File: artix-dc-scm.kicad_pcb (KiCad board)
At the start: 8 copper layers, 90 x 120.4 mm, 343 parts, among them IC1 TPS54561, J1 WE-RJ45_7499111121A, J10 61300611121, J11 DC_SOCKET, J12 S2B-PH-K-S_LF__SN_, J13 62000311121, J2 1-2199230-6, J3 543630489, J4 M20-7830642, J5 SFF-TA-1002-4C+, J6 0878311420, J7 61301021121, J8 61301021121, J9 61301221121, Q1 IRLML6402TRPBF, Q10 2N7002, Q11 2N7002, Q2 IRLML6402TRPBF, Q3 IRLML6402TRPBF, Q4 IRLML6402TRPBF, Q5 IRLML6402TRPBF, Q6 IRLML6402TRPBF, Q7 2N7002, Q8 2N7002, Q9 2N7002, U1 KSZ9031RNXCA, U10 TPS62823DLCT, U11 TPS62823DLCT, U12 TPS62823DLCT, U13 TPS62823DLCT, U14 XC7A100T-FGG484, U15 SN74LVC1G08DCKR, U15 TPS62823DLCT, U16 LM21212-2, U16 SN74LS08DBR, U2 W25Q32JVSSIQ_TR, U3 W25Q32JVSSIQ_TR, U4 W25Q32JVSSIQ_TR, U5 W25Q32JVSSIQ_TR, U6 NVT2008DQ,115, U7 AS4C256M16D3, U8 TPS51200DRC, U9 LM3881MME_NOPB, Y1 ABM8G-25.000MHZ-18-D2Y-T

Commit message: Added DDR3 and FLASH layout
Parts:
- removed the R63 at (256.4, 54.4)
- removed the R64 at (274.4, 45.2)
- removed the R65 at (271.5, 47.2)
- removed the S1 at (253.3, 87.3)
- added C48: C_4u7_0402, antmicro-footprints:0402-cap, B.Cu at (76.4, 114.8)
- added C49: C_470n_0402, antmicro-footprints:0402-cap, B.Cu at (79.8, 114.8)
- added C50: C_470n_0402, antmicro-footprints:0402-cap, B.Cu at (84.7, 121.8)
- added C91: C_47u_1210, antmicro-footprints:1210-cap, F.Cu at (187.6, 67.1)
- C35, C36, C37, C38, C51, C52, C53, C54, C55, C56, C57, C58, C59, C60, C61, C62, R21, R22, R23, R24, R25, R26, R27, R28, R29, R30, R31, R32, R33, R34, R35, R36, R37, R38, R39, R40, R41, R42, R43, R44, R60: moved to B.Cu
- R63: renamed from C48; value C_4u7_0402 -> R_1k_0402; footprint antmicro-footprints:0402-cap -> antmicro-footprints:0402-res
- R64: renamed from C49; value C_470n_0402 -> R_1k_0402; footprint antmicro-footprints:0402-cap -> antmicro-footprints:0402-res
- R65: renamed from C50; value C_470n_0402 -> R_1k_0402; footprint antmicro-footprints:0402-cap -> antmicro-footprints:0402-res
- S1: renamed from C91; value C_47u_1210 -> KMR2; footprint antmicro-footprints:1210-cap -> antmicro-footprints:SW_SPST_4.2x2.8
- moved C52 188.7 mm to (78.6, 122.2), turned to 180 degrees
- moved C58 188.6 mm to (78.3, 110.3), turned to 90 degrees
- moved R60 188.4 mm to (79.8, 112.8)
- moved C62 186.0 mm to (84.7, 115.8), turned to 90 degrees
- moved R54 184.3 mm to (72.0, 116.0), turned to 180 degrees
- moved C60 181.3 mm to (78.3, 113.0), turned to 270 degrees
- moved C61 180.9 mm to (84.7, 117.8), turned to 90 degrees
- moved R55 180.2 mm to (72.0, 121.0), turned to 180 degrees
- moved C56 180.1 mm to (78.1, 120.8), turned to 270 degrees
- moved R56 179.0 mm to (72.0, 111.0), turned to 180 degrees
- moved C59 177.6 mm to (78.3, 118.5), turned to 90 degrees
- moved R62 176.9 mm to (89.0, 116.0), turned to 180 degrees
- moved C55 176.7 mm to (84.7, 112.8), turned to 270 degrees
- moved R61 174.9 mm to (89.0, 115.0)
- moved C53 174.2 mm to (78.3, 116.5), turned to 270 degrees
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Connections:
- net /Power supply 2/VCCAUX_EN_N renamed /Power supply/VCCAUX_EN_N
- net /Power supply 2/VCCINT_EN_N renamed /Power supply/VCCINT_EN_N
- net /Power supply 2/VCCIO_EN_N renamed /Power supply/VCCIO_EN_N
- net /Power supply 2/VR1_PG renamed /Power supply/VR1_PG
- net /Power supply 2/VR2_PG renamed /Power supply/VR2_PG
- net /Power supply 2/VR_GOOD renamed /Power supply/VR_GOOD
- Q10 pad 1: /Power supply 2/1V35_PG -> /Power supply/1V35_PG
- Q11 pad 1: /Power supply 2/2V5_PG -> /Power supply/2V5_PG
- Q7 pad 1: /Power supply 2/1V0_PG -> /Power supply/1V0_PG
- Q9 pad 1: /Power supply 2/1V8_PG -> /Power supply/1V8_PG
- R63 pad 1: VCC1V35 -> VCC3V3
- R63 pad 2: GND -> /Power supply/VCCINT_EN
- R64 pad 1: VCC1V35 -> VCC3V3
- R64 pad 2: GND -> /Power supply/VCCAUX_EN
- R65 pad 1: VCC1V35 -> VCC3V3
- R65 pad 2: GND -> /Power supply/VCCIO_EN
- R91 pad 2: /Power supply 2/1V0_PG -> /Power supply/1V0_PG
- R92 pad 1: /Power supply 2/PWR_EN -> /Power supply/PWR_EN
- R93 pad 2: /Power supply 2/1V8_PG -> /Power supply/1V8_PG
- R94 pad 2: /Power supply 2/1V35_PG -> /Power supply/1V35_PG
- R95 pad 2: /Power supply 2/2V5_PG -> /Power supply/2V5_PG
- S1 pad 1: VCCB13 -> PROGRAM
- U16 pad 10: /Power supply 2/1V35_PG -> /Power supply/1V35_PG
- U16 pad 12: /Power supply 2/1V0_PG -> /Power supply/1V0_PG
- U16 pad 13: /Power supply 2/3V3_PG -> /Power supply/3V3_PG
- U16 pad 6: /Power supply 2/PWR_EN -> /Power supply/PWR_EN
- U16 pad 9: /Power supply 2/1V8_PG -> /Power supply/1V8_PG
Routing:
- net VCC3V3: track 8.31 -> 20.1 mm, vias 3 -> 7
- net VCC1V35: track 2.88 -> 14.6 mm, vias 0 -> 6
- net QSPIB_CLK: track 0.00 -> 11.2 mm, vias 0 -> 2
- net QSPIA_CLK: track 0.00 -> 11.2 mm, vias 0 -> 2
- net GND: track 10.0 -> 19.6 mm, vias 0 -> 5
- net QSPIB2_CS_N: track 0.00 -> 9.11 mm, vias 0 -> 1
- net QSPIA2_CS_N: track 0.00 -> 8.10 mm, vias 0 -> 1
- net QSPIB1_CS_N: track 0.00 -> 8.10 mm, vias 0 -> 1
- net QSPIA1_CS_N: track 0.00 -> 8.10 mm, vias 0 -> 1
- net QSPIB2_D3: track 0.00 -> 7.56 mm, vias 0 -> 1
- net QSPIB1_D3: track 0.00 -> 7.56 mm, vias 0 -> 1
- net QSPIA2_D3: track 0.00 -> 7.56 mm, vias 0 -> 1
- net QSPIA1_D3: track 0.00 -> 7.56 mm, vias 0 -> 1
- net QSPIB2_D1: track 0.00 -> 6.41 mm, vias 0 -> 1
- net QSPIB1_D1: track 0.00 -> 6.41 mm, vias 0 -> 1
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
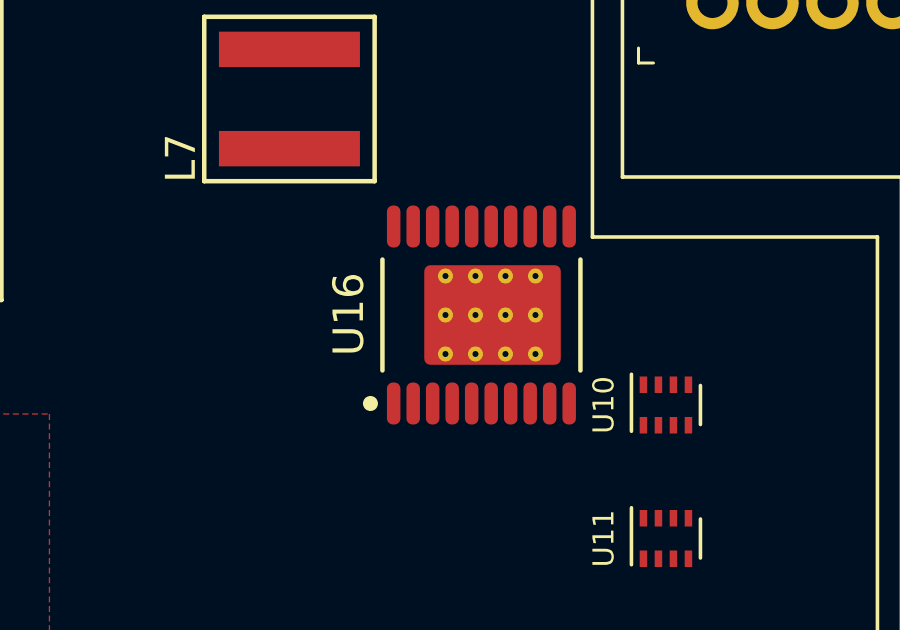
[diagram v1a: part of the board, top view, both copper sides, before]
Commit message: Updated board 3D models
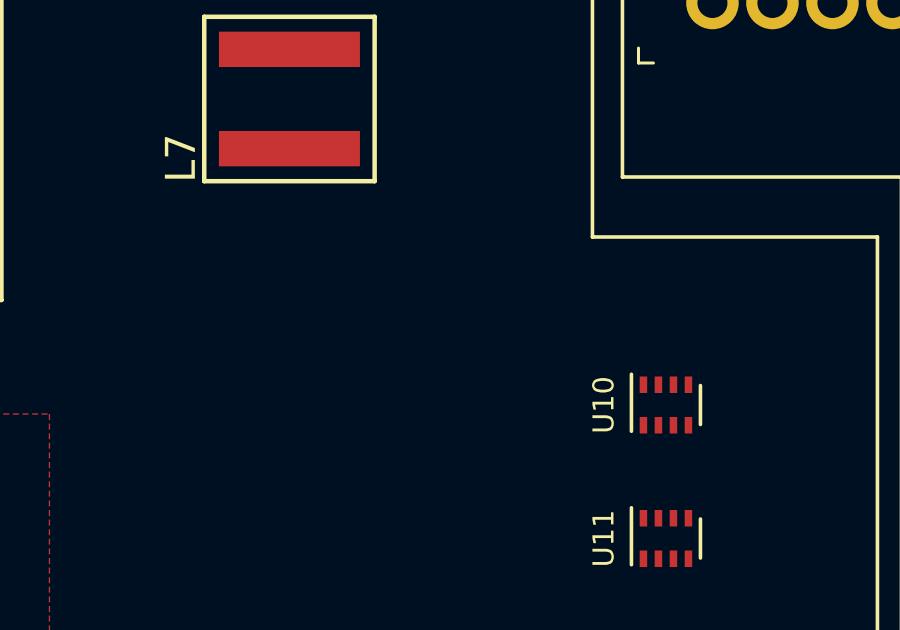
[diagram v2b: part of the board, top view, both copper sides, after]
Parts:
- removed the U16 at (92.3, 74.1)
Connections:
- J2 pad 1: GND -> (no net)
- J2 pad 10: Net-(D1-Pad2) -> (no net)
- J2 pad 11: Net-(J2-Pad11) -> (no net)
- J2 pad 12: VCC3V3 -> (no net)
- J2 pad 13: Net-(J2-Pad13) -> (no net)
- J2 pad 14: VCC3V3 -> (no net)
- J2 pad 15: GND -> (no net)
- J2 pad 16: VCC3V3 -> (no net)
- J2 pad 17: Net-(J2-Pad17) -> (no net)
- J2 pad 18: VCC3V3 -> (no net)
- J2 pad 19: Net-(J2-Pad19) -> (no net)
- J2 pad 2: VCC3V3 -> (no net)
- J2 pad 20: Net-(J2-Pad20) -> (no net)
- J2 pad 21: GND -> (no net)
- J2 pad 22: Net-(J2-Pad22) -> (no net)
- J2 pad 23: Net-(J2-Pad23) -> (no net)
- J2 pad 24: Net-(J2-Pad24) -> (no net)
- J2 pad 25: Net-(J2-Pad25) -> (no net)
- J2 pad 26: Net-(J2-Pad26) -> (no net)
- J2 pad 27: GND -> (no net)
- J2 pad 28: Net-(J2-Pad28) -> (no net)
- J2 pad 29: Net-(J2-Pad29) -> (no net)
- J2 pad 3: GND -> (no net)
- J2 pad 30: Net-(J2-Pad30) -> (no net)
- J2 pad 31: Net-(J2-Pad31) -> (no net)
- J2 pad 32: Net-(J2-Pad32) -> (no net)
- J2 pad 33: GND -> (no net)
- J2 pad 34: Net-(J2-Pad34) -> (no net)
- J2 pad 35: Net-(C30-Pad1) -> (no net)
- J2 pad 36: Net-(J2-Pad36) -> (no net)
- J2 pad 37: Net-(C28-Pad1) -> (no net)
- J2 pad 38: Net-(J2-Pad38) -> (no net)
- J2 pad 39: GND -> (no net)
- J2 pad 4: VCC3V3 -> (no net)
- J2 pad 40: Net-(J2-Pad40) -> (no net)
- J2 pad 41: PCIE_HPM_RXN[0] -> (no net)
- J2 pad 42: Net-(J2-Pad42) -> (no net)
- J2 pad 43: PCIE_HPM_RXP[0] -> (no net)
- J2 pad 44: Net-(J2-Pad44) -> (no net)
- J2 pad 45: GND -> (no net)
- J2 pad 46: Net-(J2-Pad46) -> (no net)
- J2 pad 47: Net-(C29-Pad1) -> (no net)
- J2 pad 48: Net-(J2-Pad48) -> (no net)
- J2 pad 49: Net-(C27-Pad1) -> (no net)
- J2 pad 5: Net-(J2-Pad5) -> (no net)
- J2 pad 50: PEX_L0_RST_N -> (no net)
- J2 pad 51: GND -> (no net)
- J2 pad 52: PEX_L0_CLKREQ_N -> (no net)
- J2 pad 53: CLK_100M_PCIE_DN -> (no net)
- J2 pad 54: PEWAKE_3V3_N -> (no net)
- J2 pad 55: CLK_100M_PCIE_DP -> (no net)
- J2 pad 56: Net-(J2-Pad56) -> (no net)
- J2 pad 57: GND -> (no net)
- J2 pad 58: Net-(J2-Pad58) -> (no net)
- J2 pad 6: Net-(J2-Pad6) -> (no net)
- J2 pad 67: Net-(J2-Pad67) -> (no net)
- J2 pad 68: Net-(J2-Pad68) -> (no net)
- J2 pad 69: Net-(J2-Pad69) -> (no net)
- J2 pad 7: Net-(J2-Pad7) -> (no net)
- J2 pad 70: VCC3V3 -> (no net)
- J2 pad 71: GND -> (no net)
- J2 pad 72: VCC3V3 -> (no net)
- J2 pad 73: GND -> (no net)
- J2 pad 74: VCC3V3 -> (no net)
- J2 pad 75: GND -> (no net)
- J2 pad 8: Net-(J2-Pad8) -> (no net)
- J2 pad 9: GND -> (no net)
- J2 pad SH1: GND -> (no net)
- J2 pad SH2: GND -> (no net)

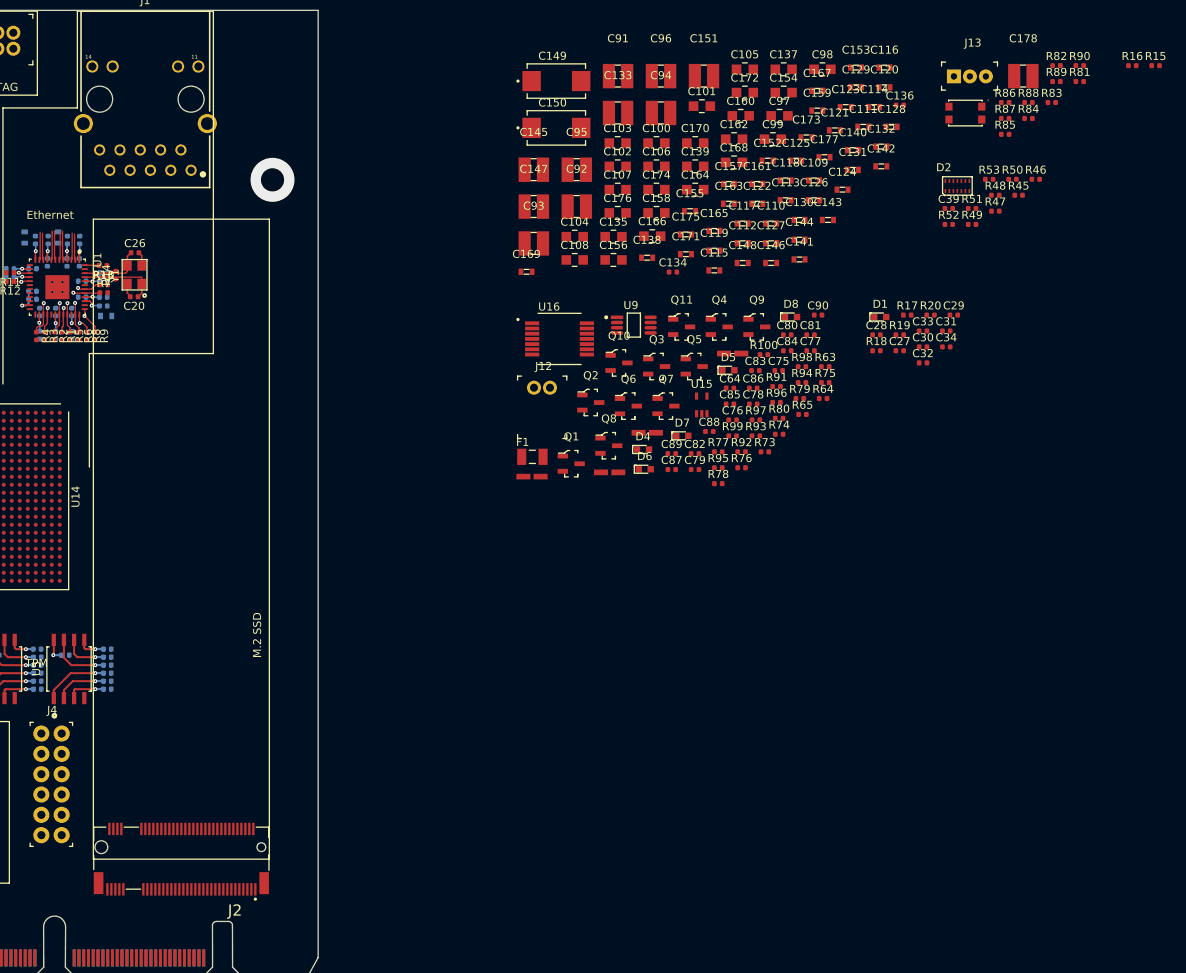
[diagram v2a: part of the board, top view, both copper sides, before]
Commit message: Added M.2 connector layout
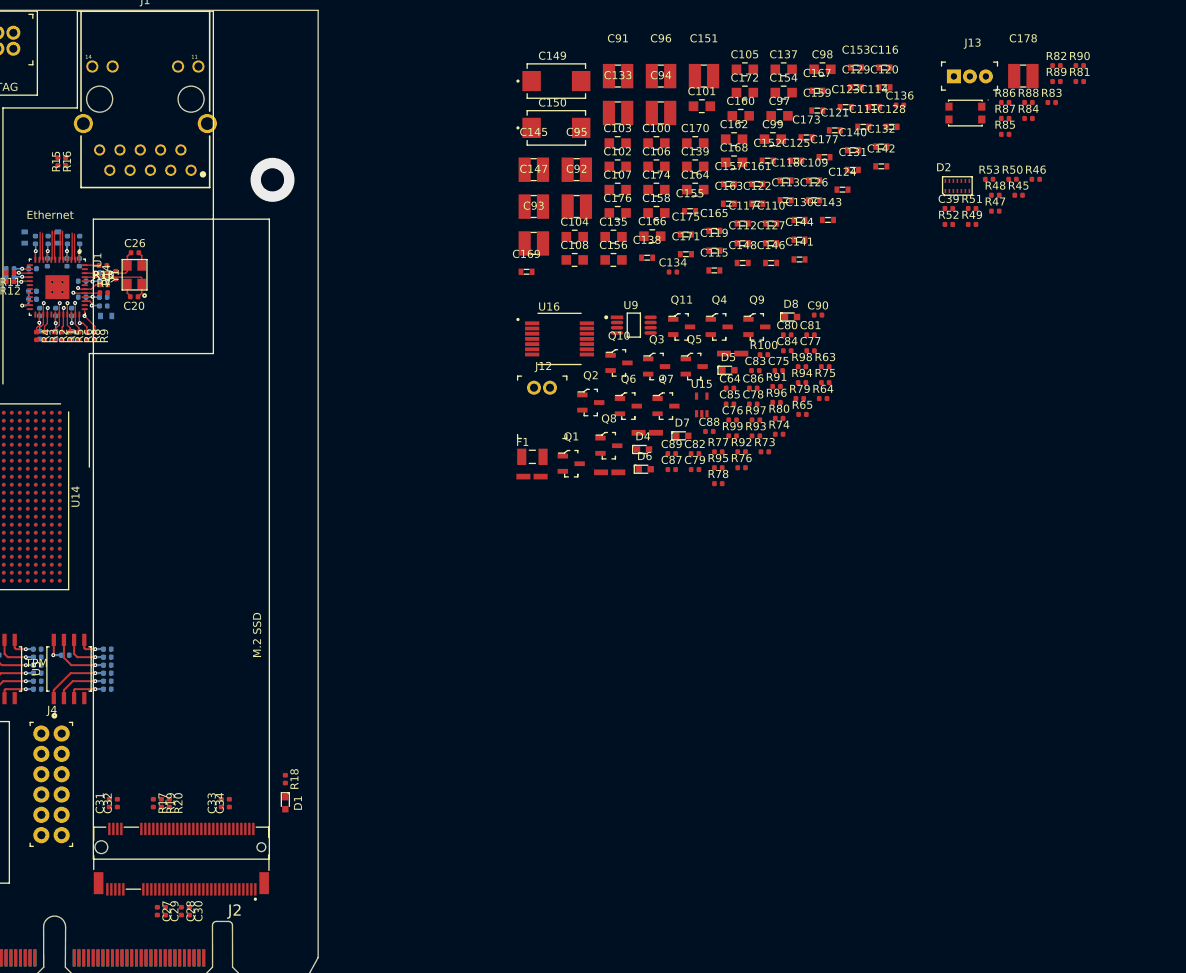
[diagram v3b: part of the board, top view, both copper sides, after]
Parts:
- moved R15 136.8 mm to (118.5, 77.8), turned to 90 degrees
- moved R16 134.8 mm to (117.6, 77.8), turned to 270 degrees
- moved C29 123.6 mm to (131.0, 171.5), turned to 270 degrees
- moved C31 120.1 mm to (124.0, 158.0), turned to 90 degrees
- moved C27 116.3 mm to (130.0, 171.5), turned to 270 degrees
- moved C30 115.7 mm to (134.0, 171.5), turned to 270 degrees
- moved C32 114.8 mm to (125.0, 158.0), turned to 90 degrees
- moved R20 113.0 mm to (131.5, 158.0), turned to 270 degrees
- moved C28 112.9 mm to (133.0, 171.5), turned to 270 degrees
- moved R17 112.3 mm to (129.5, 158.0), turned to 270 degrees
- moved R19 109.3 mm to (130.5, 158.0), turned to 270 degrees
- moved C34 106.2 mm to (139.0, 158.0), turned to 90 degrees
- moved C33 105.7 mm to (138.0, 158.0), turned to 90 degrees
- moved D1 96.0 mm to (146.0, 158.0), turned to 270 degrees
- moved R18 91.3 mm to (146.0, 155.0), turned to 270 degrees
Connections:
- J2 pad 1: (no net) -> GND
- J2 pad 10: (no net) -> Net-(D1-Pad2)
- J2 pad 11: (no net) -> Net-(J2-Pad11)
- J2 pad 12: (no net) -> VCC3V3
- J2 pad 13: (no net) -> Net-(J2-Pad13)
- J2 pad 14: (no net) -> VCC3V3
- J2 pad 15: (no net) -> GND
- J2 pad 16: (no net) -> VCC3V3
- J2 pad 17: (no net) -> Net-(J2-Pad17)
- J2 pad 18: (no net) -> VCC3V3
- J2 pad 19: (no net) -> Net-(J2-Pad19)
- J2 pad 2: (no net) -> VCC3V3
- J2 pad 20: (no net) -> Net-(J2-Pad20)
- J2 pad 21: (no net) -> GND
- J2 pad 22: (no net) -> Net-(J2-Pad22)
- J2 pad 23: (no net) -> Net-(J2-Pad23)
- J2 pad 24: (no net) -> Net-(J2-Pad24)
- J2 pad 25: (no net) -> Net-(J2-Pad25)
- J2 pad 26: (no net) -> Net-(J2-Pad26)
- J2 pad 27: (no net) -> GND
- J2 pad 28: (no net) -> Net-(J2-Pad28)
- J2 pad 29: (no net) -> Net-(J2-Pad29)
- J2 pad 3: (no net) -> GND
- J2 pad 30: (no net) -> Net-(J2-Pad30)
- J2 pad 31: (no net) -> Net-(J2-Pad31)
- J2 pad 32: (no net) -> Net-(J2-Pad32)
- J2 pad 33: (no net) -> GND
- J2 pad 34: (no net) -> Net-(J2-Pad34)
- J2 pad 35: (no net) -> Net-(C30-Pad1)
- J2 pad 36: (no net) -> Net-(J2-Pad36)
- J2 pad 37: (no net) -> Net-(C28-Pad1)
- J2 pad 38: (no net) -> Net-(J2-Pad38)
- J2 pad 39: (no net) -> GND
- J2 pad 4: (no net) -> VCC3V3
- J2 pad 40: (no net) -> Net-(J2-Pad40)
- J2 pad 41: (no net) -> PCIE_HPM_RXN[0]
- J2 pad 42: (no net) -> Net-(J2-Pad42)
- J2 pad 43: (no net) -> PCIE_HPM_RXP[0]
- J2 pad 44: (no net) -> Net-(J2-Pad44)
- J2 pad 45: (no net) -> GND
- J2 pad 46: (no net) -> Net-(J2-Pad46)
- J2 pad 47: (no net) -> Net-(C29-Pad1)
- J2 pad 48: (no net) -> Net-(J2-Pad48)
- J2 pad 49: (no net) -> Net-(C27-Pad1)
- J2 pad 5: (no net) -> Net-(J2-Pad5)
- J2 pad 50: (no net) -> PEX_L0_RST_N
- J2 pad 51: (no net) -> GND
- J2 pad 52: (no net) -> PEX_L0_CLKREQ_N
- J2 pad 53: (no net) -> CLK_100M_PCIE_DN
- J2 pad 54: (no net) -> PEWAKE_3V3_N
- J2 pad 55: (no net) -> CLK_100M_PCIE_DP
- J2 pad 56: (no net) -> Net-(J2-Pad56)
- J2 pad 57: (no net) -> GND
- J2 pad 58: (no net) -> Net-(J2-Pad58)
- J2 pad 6: (no net) -> Net-(J2-Pad6)
- J2 pad 67: (no net) -> Net-(J2-Pad67)
- J2 pad 68: (no net) -> Net-(J2-Pad68)
- J2 pad 69: (no net) -> Net-(J2-Pad69)
- J2 pad 7: (no net) -> Net-(J2-Pad7)
- J2 pad 70: (no net) -> VCC3V3
- J2 pad 71: (no net) -> GND
- J2 pad 72: (no net) -> VCC3V3
- J2 pad 73: (no net) -> GND
- J2 pad 74: (no net) -> VCC3V3
- J2 pad 75: (no net) -> GND
- J2 pad 8: (no net) -> Net-(J2-Pad8)
- J2 pad 9: (no net) -> GND
- J2 pad SH1: (no net) -> GND
- J2 pad SH2: (no net) -> GND
